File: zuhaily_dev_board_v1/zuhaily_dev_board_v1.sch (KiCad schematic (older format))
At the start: 54 parts

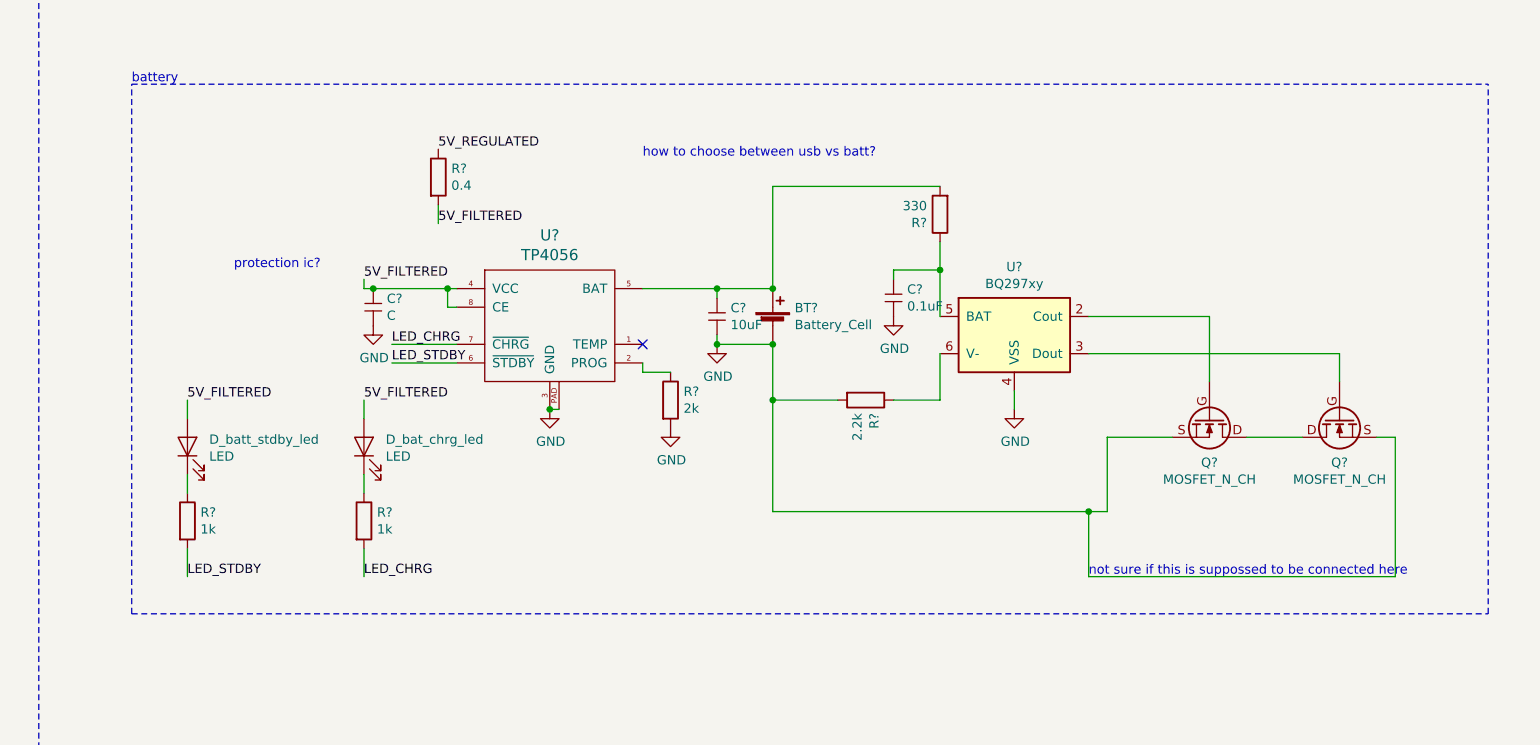
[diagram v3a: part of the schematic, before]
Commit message: added battery protection - dwa01
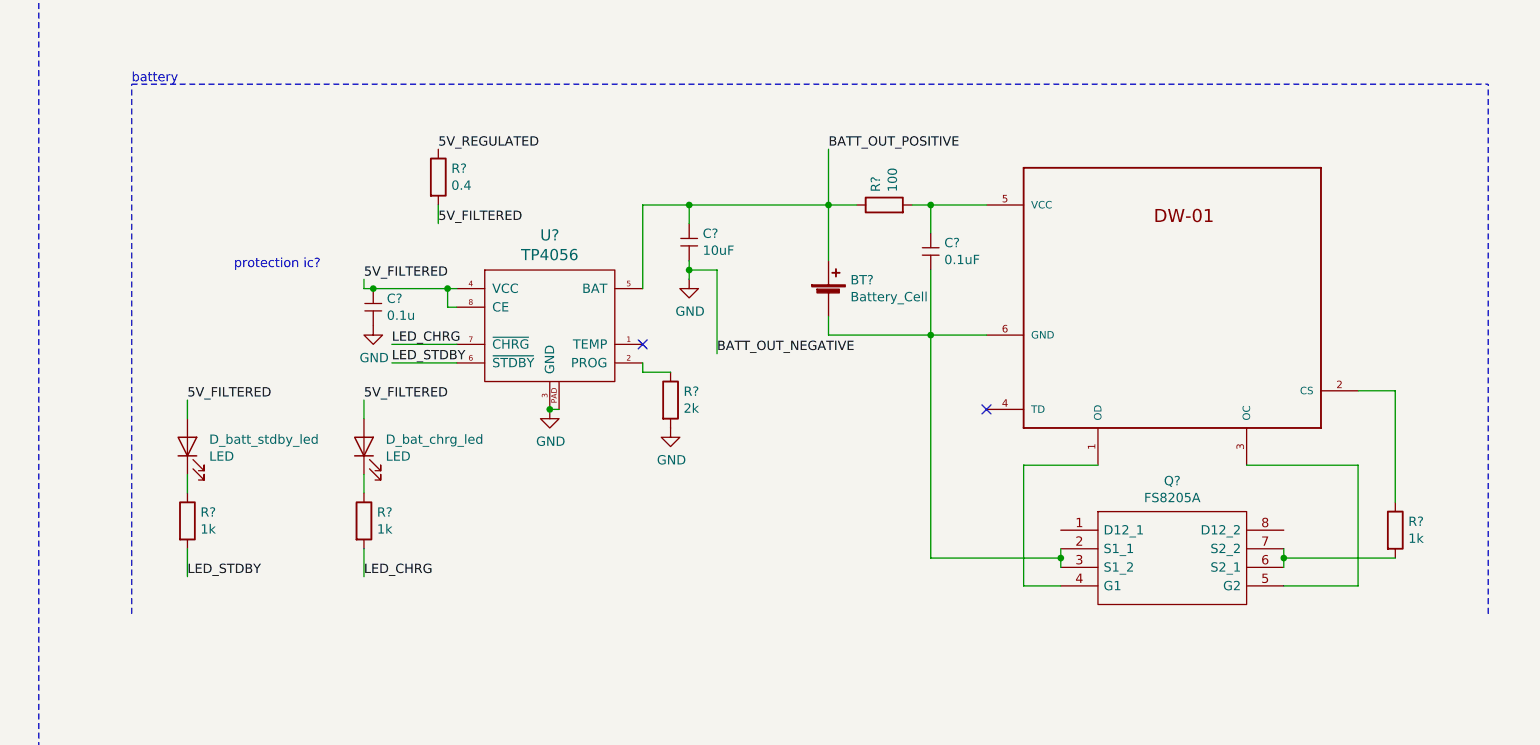
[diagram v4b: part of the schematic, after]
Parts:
- removed BT?: Battery_Cell, symbol Device:Battery_Cell
- removed C?: 10uF, symbol c:C
- removed C?: 0.1uF, symbol c:C
- removed Q? (x2): MOSFET_N_CH, symbol tinkerforge:MOSFET_N_CH
- removed R?: 2.2k, symbol Device:R
- removed R?: 330, symbol Device:R
- removed U?: BQ297xy, Package_SON:WSON-6_1.5x1.5mm_P0.5mm, symbol Battery_Management:BQ297xy
- added BT?: Battery_Cell, symbol Device:Battery_Cell
- added C?: 10uF, symbol c:C
- added C?: 0.1uF, symbol c:C
- added Q?: FS8205A, SOP65P640X120-8N, symbol FS8205A:FS8205A
- added R?: 1k, symbol Device:R
- added R?: 100, symbol Device:R
- added U?: DW-01, SOT23-6, symbol DW-01:DW-01
- C?: value C -> 0.1u
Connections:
- net GND: now also C?.2
- net BATT_OUT_POSITIVE: now reaches U?.5 (BAT)
- net BATT_OUT_POSITIVE: now also BT?.1 (+), C?.1, R?.1
- new net: Q?.4 (G1), U?.1 (OD)
- new net: R?.1, U?.2 (CS)
- new net: Q?.5 (G2), U?.3 (OC)
- new net: C?.1, R?.2, U?.5 (VCC)
- new net: BT?.2 (-), C?.2, Q?.2 (S1_1), Q?.3 (S1_2), U?.6 (GND)
- new net: Q?.6 (S2_1), Q?.7 (S2_2), R?.2
- no-connect marks 1 -> 2
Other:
- note removed: "how to choose between usb vs batt?\n"
- note removed: "not sure if this is suppossed to be connected here\n"

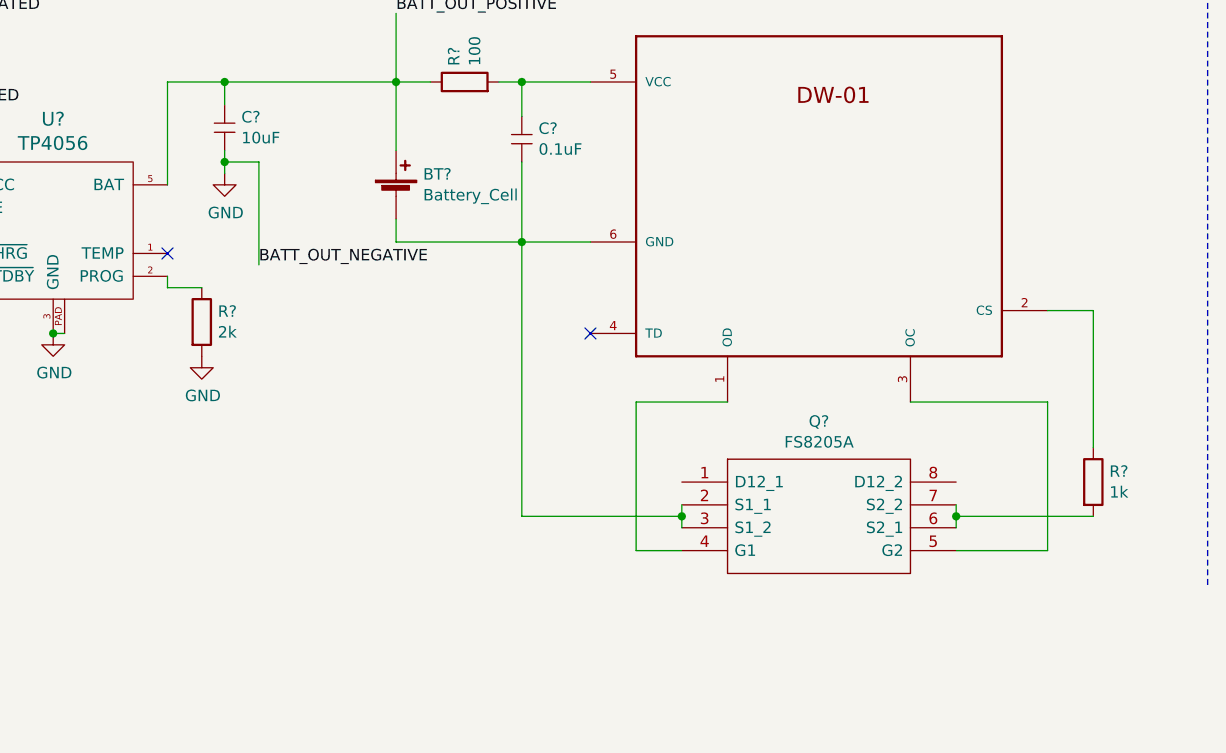
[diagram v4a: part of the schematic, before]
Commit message: corrected some changes in the battery protect circuit
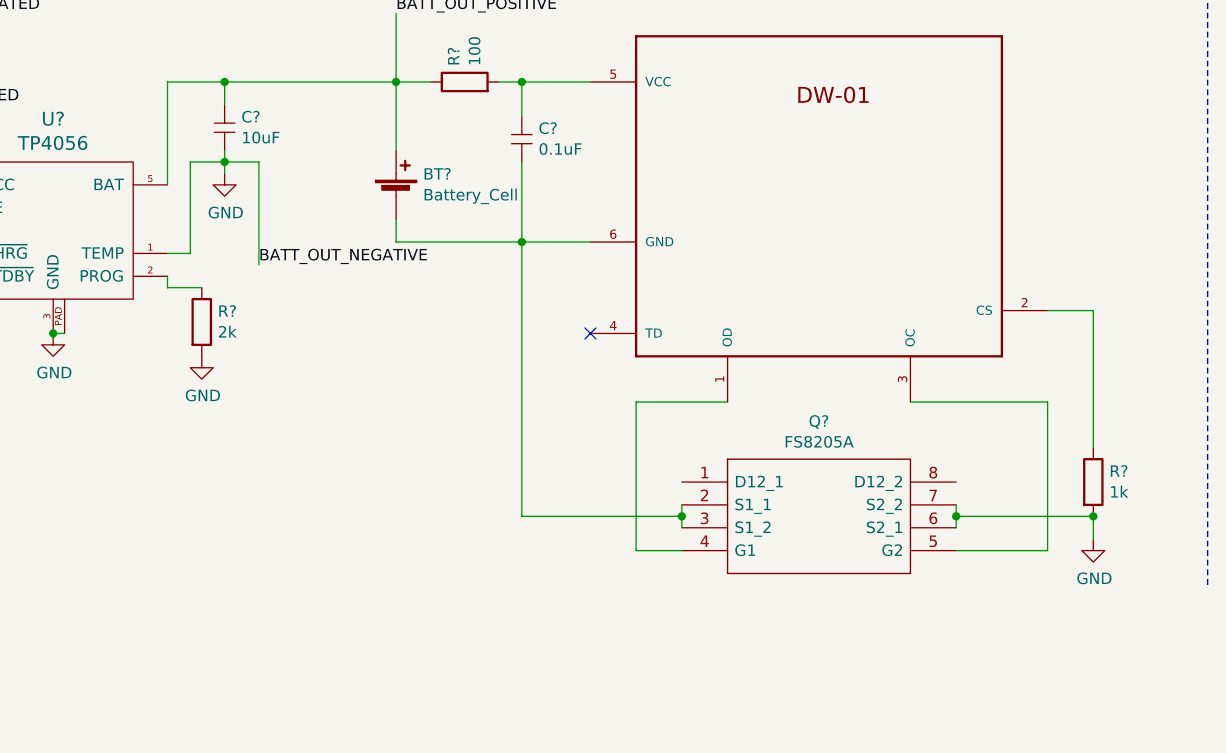
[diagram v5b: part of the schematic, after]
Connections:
- net GND: now also Q?.6 (S2_1), Q?.7 (S2_2), R?.2, U?.1 (TEMP)
- no-connect marks 2 -> 1
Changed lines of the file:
@@
 	15450 6400 15450 6600
 Connection ~ 15200 6400
-NoConn ~ 17300 3550
 $Comp
 L pspice:DIODE D?
@@
 	18300 2500 18300 2800
 NoConn ~ 19150 3900
+$Comp
+L power:GND #PWR?
+U 1 1 5C82DB1B
+P 21350 4800
+F 0 "#PWR?" H 21350 4550 50  0001 C CNN
+F 1 "GND" H 21355 4627 50  0000 C CNN
+F 2 "" H 21350 4800 50  0001 C CNN
+F 3 "" H 21350 4800 50  0001 C CNN
+	1    21350 4800
+	1    0    0    -1
+$EndComp
+Wire Wire Line
+	21350 4800 21350 4700
+Connection ~ 21350 4700
+Wire Wire Line
+	17300 3550 17400 3550
+Wire Wire Line
+	17400 3550 17400 3150
+Wire Wire Line
+	17400 3150 17550 3150
 $EndSCHEMATC

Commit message: finished schematic started pcb design
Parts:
- added D3: D, Diode_SMD:D_1206_3216Metric_Pad1.42x1.75mm_HandSolder, symbol d:D
- added unit 3 of U8
- BT1: renamed from BT?; footprint (none) -> Battery:BatteryHolder_MPD_BH-18650-PC2
- C1, C2: renamed from C?; value C -> 22pF; footprint (none) -> Capacitor_THT:C_Disc_D4.7mm_W2.5mm_P5.00mm
- C10, C11, C12, C4, C5, C6, C7: renamed from C?; footprint (none) -> Capacitor_THT:CP_Radial_D5.0mm_P2.50mm
- C3: renamed from C?; value C -> 0.1uF; footprint (none) -> Capacitor_SMD:CP_Elec_4x3.9
- C8, C9: renamed from C?; footprint (none) -> Capacitor_THT:C_Disc_D4.7mm_W2.5mm_P5.00mm
- D1: renamed from D?; footprint (none) -> LED_SMD:LED_1206_3216Metric
- D2: renamed from D?; footprint (none) -> Diode_SMD:D_1206_3216Metric_Pad1.42x1.75mm_HandSolder
- D_arduino_rx_led1: renamed from D_arduino_rx_led; footprint (none) -> LED_SMD:LED_1206_3216Metric_Pad1.42x1.75mm_HandSolder
- D_arduino_tx_led1: renamed from D_arduino_tx_led; footprint (none) -> LED_SMD:LED_1206_3216Metric_Pad1.42x1.75mm_HandSolder
- D_bat_chrg_led1: renamed from D_bat_chrg_led; footprint (none) -> LED_SMD:LED_1206_3216Metric_Pad1.42x1.75mm_HandSolder
- D_batt_stdby_led1: renamed from D_batt_stdby_led; footprint (none) -> LED_SMD:LED_1206_3216Metric_Pad1.42x1.75mm_HandSolder
- J1: renamed from J?; footprint (none) -> Connector_USB:USB_Micro-B_Wuerth_629105150521_CircularHoles
- J2: renamed from J?; footprint (none) -> Connector_Card:microSD_HC_Hirose_DM3D-SF
- J3: renamed from J?; footprint (none) -> Connector_BarrelJack:BarrelJack_Horizontal
- J_oled_header1: renamed from J_oled_header; footprint (none) -> Connector:FanPinHeader_1x04_P2.54mm_Vertical
- Q1: renamed from Q?; footprint SOP65P640X120-8N -> FS8205A:SOP65P640X120-8N
- Q_FDN340P1: renamed from Q_FDN340P; footprint (none) -> Package_TO_SOT_SMD:SOT-323_SC-70
- R1: renamed from R?; footprint (none) -> Package_TO_SOT_SMD:SuperSOT-3
- R10, R11: renamed from R?; footprint (none) -> Resistor_THT:R_Axial_DIN0204_L3.6mm_D1.6mm_P5.08mm_Horizontal
- R12, R13, R14, R2, R3, R4, R5, R6, R7, R8: renamed from R?; footprint (none) -> Resistor_THT:R_Axial_DIN0207_L6.3mm_D2.5mm_P7.62mm_Horizontal
- R9: renamed from R?; footprint (none) -> Resistor_THT:R_Axial_DIN0414_L11.9mm_D4.5mm_P15.24mm_Horizontal
- SW1: renamed from SW?; footprint (none) -> Button_Switch_THT:SW_E-Switch_EG1271_DPDT
- SW2: renamed from SW?; footprint (none) -> Button_Switch_THT:SW_PUSH_6mm_H4.3mm
- U1: renamed from U?; footprint (none) -> Package_DIP:DIP-20_W7.62mm_Socket_LongPads
- U10: renamed from U?; footprint SOT23-6 -> DW-01:SOT23-6
- U2, U4: renamed from U?; footprint (none) -> Package_TO_SOT_SMD:SOT-89-3
- U3: renamed from U?; footprint Package_SO:SOIC-16_3.9x9.9mm_P1.27mm -> Package_SO:SSOP-20_5.3x7.2mm_P0.65mm
- U5: renamed from U?; footprint Package_DIP:DIP-28_W7.62mm -> Module:Arduino_UNO_R3
- U6: renamed from U?; footprint (none) -> Connector_PinHeader_2.54mm:PinHeader_2x04_P2.54mm_Vertical
- U7: renamed from U?; footprint (none) -> Package_SO:HSOP-8-1EP_3.9x4.9mm_P1.27mm_EP2.41x3.1mm
- U8: renamed from U?; footprint (none) -> Package_SO:TSSOP-8_3x3mm_P0.65mm
- Y1, Y2: renamed from Y?; footprint (none) -> Crystal:Crystal_HC49-4H_Vertical
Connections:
- net 5V_REGULATED: now also D3.C
- net BATT_OUT_POSITIVE: now also D3.A
- net GND: now also J1.6 (Shield)
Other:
- note removed: "also not sure why vin is divided by 2\n"
- note removed: "not sure why it's compared to 3.3v\n"

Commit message: generated pcb
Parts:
- removed C10: 0.1u, Capacitor_THT:CP_Radial_D5.0mm_P2.50mm, symbol c:C
- removed C11: 10uF, Capacitor_THT:CP_Radial_D5.0mm_P2.50mm, symbol c:C
- removed C12: 0.1uF, Capacitor_THT:CP_Radial_D5.0mm_P2.50mm, symbol c:C
- removed C3: 0.1uF, Capacitor_SMD:CP_Elec_4x3.9, symbol c:C
- removed C4: 47uF, Capacitor_THT:CP_Radial_D5.0mm_P2.50mm, symbol c:C
- removed C5, C6: 100nF, Capacitor_THT:CP_Radial_D5.0mm_P2.50mm, symbol c:C
- removed C7: C, Capacitor_THT:CP_Radial_D5.0mm_P2.50mm, symbol c:C
- removed D2: DIODE, Diode_SMD:D_1206_3216Metric_Pad1.42x1.75mm_HandSolder, symbol pspice:DIODE
- removed D3: D, Diode_SMD:D_1206_3216Metric_Pad1.42x1.75mm_HandSolder, symbol d:D
- removed J2: SD_Card, Connector_Card:microSD_HC_Hirose_DM3D-SF, symbol Connector:SD_Card
- removed Q_FDN340P1: MOSFET_P_CH, Package_TO_SOT_SMD:SOT-323_SC-70, symbol tinkerforge:MOSFET_P_CH
- removed R9: 0.4, Resistor_THT:R_Axial_DIN0414_L11.9mm_D4.5mm_P15.24mm_Horizontal, symbol Device:R
- added C10, C12, C3, C7: 0.1uF, Capacitor_THT:CP_Radial_D5.0mm_P2.50mm, symbol Device:CP_Small
- added C11: 10uF, Capacitor_THT:CP_Radial_D5.0mm_P2.50mm, symbol Device:CP_Small
- added C4: 47uF, Capacitor_THT:CP_Radial_D5.0mm_P2.50mm, symbol Device:CP_Small
- added C5, C6: 100nF, Capacitor_THT:CP_Radial_D5.0mm_P2.50mm, symbol Device:CP_Small
- added D2, D3: D, Diode_SMD:D_1206_3216Metric_Pad1.42x1.75mm_HandSolder, symbol Device:D
- added J2: Micro_SD_Card, sd_card_pretty:Conn_uSDcard, symbol Connector:Micro_SD_Card
- added J4: Conn_01x32_Female, Module:Arduino_UNO_R3, symbol Connector:Conn_01x32_Female
- added Q2: FDN340P, Package_TO_SOT_SMD:SOT-323_SC-70, symbol FDN340P:FDN340P
- added SW3, SW4, SW5: SW_DIP_x04, Button_Switch_THT:SW_DIP_SPSTx04_Slide_9.78x12.34mm_W7.62mm_P2.54mm, symbol Switch:SW_DIP_x04
- BT1: footprint Battery:BatteryHolder_MPD_BH-18650-PC2 -> Battery:BatteryHolder_Keystone_1042_1x18650
- R1: footprint Package_TO_SOT_SMD:SuperSOT-3 -> Resistor_THT:R_Axial_DIN0207_L6.3mm_D2.5mm_P7.62mm_Horizontal
- R10, R11: footprint Resistor_THT:R_Axial_DIN0204_L3.6mm_D1.6mm_P5.08mm_Horizontal -> Resistor_THT:R_Axial_DIN0207_L6.3mm_D2.5mm_P7.62mm_Horizontal
- U1: footprint Package_DIP:DIP-20_W7.62mm_Socket_LongPads -> Package_SO:SOIC-20W_7.5x12.8mm_P1.27mm
- U2, U4: footprint Package_TO_SOT_SMD:SOT-89-3 -> Package_TO_SOT_SMD:SOT-223
- U3: footprint Package_SO:SSOP-20_5.3x7.2mm_P0.65mm -> Package_SO:SOP-16_4.4x10.4mm_P1.27mm
- U5: footprint Module:Arduino_UNO_R3 -> Package_DIP:DIP-28_W7.62mm_Socket_LongPads
- renumbered U6 to U_ESP1
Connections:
- net 5V_REGULATED is gone; now on net 5V_FILTERED: D1.2 (A), R4.1, R5.2, R6.1, U2.2 (VO), U3.16 (VCC), U4.3 (VI), U5.20 (AVCC), U5.21 (AREF), U5.7 (VCC)
- net 3.3V_REGULATED: now also J2.4 (VDD), J4.4 (Pin_4), SW4.3; no longer U_ESP1.7 (VCC)
- net 5V_FILTERED: now also U8.8 (V+), C10.1, C3.1, C4.1, C5.1, C6.1, D3.1 (K), J4.2 (Pin_2), J4.30 (Pin_30), J4.5 (Pin_5), J4.8 (Pin_8), Q2.3 (D), SW5.1
- net 5V_REGULATOR_IN: now also D2.1 (K)
- net ARDUINO_LEVEL_SHIFT_CS: now also J4.25 (Pin_25), SW3.2; no longer U1.6 (A4)
- net ARDUINO_LEVEL_SHIFT_MOSI: now also J4.26 (Pin_26), SW3.3; no longer U1.7 (A5)
- net ARDUINO_LEVEL_SHIFT_SCK: now also J4.28 (Pin_28), SW3.1; no longer U1.5 (A3)
- net ARDUINO_RESET: now also C7.2, J4.3 (Pin_3)
- net ARDUINO_RX: now also U5.2 (PD0), J4.15 (Pin_15)
- net ARDUINO_SD_MISO: now also J4.27 (Pin_27), SW3.4
- net ARDUINO_TX: now also U5.3 (PD1), J4.16 (Pin_16)
- net BATT_OUT_POSITIVE: now also C11.1, D3.2 (A)
- net CH340_DTR: now also C7.1
- net ESP_RX: now also SW4.2; no longer U_ESP1.8 (URXD)
- net ESP_TX: now also SW4.1; no longer U_ESP1.1 (UTXD)
- net GND: now also U8.4 (V-), C10.2, C11.2, C4.2, C5.2, C6.2, J2.6 (VSS), J2.9 (SHIELD), J4.29 (Pin_29), J4.6 (Pin_6), J4.7 (Pin_7), SW4.4, SW5.2; no longer U_ESP1.2 (GND)
- net LEVEL_SHIFT_SD_CS: now also J2.2 (DAT3/CD)
- net LEVEL_SHIFT_SD_MOSI: now also J2.3 (CMD)
- net LEVEL_SHIFT_SD_SCK: now also J2.5 (CLK)
- net USB_VCC: now also Q2.2 (S)
- net PD_5: now reaches U5.11 (PD5)
- net PD_5: now also J4.20 (Pin_20)
- net PD_6: now reaches U5.12 (PD6)
- net PD_6: now also J4.21 (Pin_21)
- net PD_7: now reaches U5.13 (PD7)
- net PD_7: now also J4.22 (Pin_22)
- net PB_0: now reaches U5.14 (PB0)
- net PB_0: now also J4.23 (Pin_23)
- net PB_1: now reaches U5.15 (PB1)
- net PB_1: now also J4.24 (Pin_24)
- net PC_0: now reaches U5.23 (PC0)
- net PC_0: now also J4.9 (Pin_9)
- net PC_1: now reaches U5.24 (PC1)
- net PC_1: now also J4.10 (Pin_10)
- net PC_2: now reaches U5.25 (PC2)
- net PC_2: now also J4.11 (Pin_11)
- net PC_3: now reaches U5.26 (PC3)
- net PC_3: now also J4.12 (Pin_12)
- net PC_4: now reaches U5.27 (PC4)
- net PC_4: now also J4.13 (Pin_13), J4.31 (Pin_31), SW5.4
- net PC_5: now reaches U5.28 (PC5)
- net PC_5: now also J4.14 (Pin_14), J4.32 (Pin_32), SW5.3
- net PD_2: now reaches U5.4 (PD2)
- net PD_2: now also J4.17 (Pin_17)
- net PD_3: now reaches U5.5 (PD3)
- net PD_3: now also J4.18 (Pin_18)
- net PD_4: now reaches U5.6 (PD4)
- net PD_4: now also J4.19 (Pin_19)
- net at U3.4 (V3): now also C3.2
- net at J3.2: now also D2.2 (A)
- net at J_oled_header1.1 (Pin_1): now also SW5.5
- net at J_oled_header1.2 (Pin_2): now also SW5.6
- net at J_oled_header1.3 (Pin_3): now also SW5.7
- net at J_oled_header1.4 (Pin_4): now also SW5.8
- net at U8.1: now also Q2.1 (G)
- net at R13.2, U10.5 (VCC): now also C12.1
- net at BT1.2 (-), Q1.2 (S1_1), Q1.3 (S1_2)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: now also C12.2
- new net: SW3.8, U1.5 (A3)
- new net: SW3.7, U1.6 (A4)
- new net: SW3.6, U1.7 (A5)
- new net: SW4.8, U_ESP1.1 (UTXD)
- new net: SW4.5, U_ESP1.2 (GND)
- new net: SW4.6, U_ESP1.7 (VCC)
- new net: SW4.7, U_ESP1.8 (URXD)
- new net: J2.7 (DAT0), SW3.5
- no-connect marks 1 -> 4
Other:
- note added: "You can put a 0.4 ohm resistor, recommended in the datasheet but I didn't\n"
- note removed: "pullup resistors?\n"
- moved on the sheet: C8, C9, D_arduino_rx_led1, D_arduino_tx_led1, J_oled_header1, R4, R5, R6, SW2, Y2

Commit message: changed battery holder
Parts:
- BT1: footprint Battery:BatteryHolder_Keystone_1042_1x18650 -> Battery:BatteryHolder_MPD_BH-18650-PC2
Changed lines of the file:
@@
 F 0 "BT1" H 18418 3396 50  0000 L CNN
 F 1 "Battery_Cell" H 18418 3305 50  0000 L CNN
-F 2 "Battery:BatteryHolder_Keystone_1042_1x18650" V 18300 3360 50  0001 C CNN
+F 2 "Battery:BatteryHolder_MPD_BH-18650-PC2" V 18300 3360 50  0001 C CNN
 F 3 "~" V 18300 3360 50  0001 C CNN
 	1    18300 3300
